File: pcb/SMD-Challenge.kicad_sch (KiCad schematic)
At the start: 1 part

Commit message: Add first draft
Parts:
- removed R?: (no value), symbol Device:R
- added BT1: Battery_Cell, Battery:BatteryHolder_Keystone_3002_1x2032, symbol Device:Battery_Cell
- added C1: 1u, Capacitor_SMD:C_1206_3216Metric, symbol Device:C
- added D1, D2: LED, LED_SMD:LED_1206_3216Metric, symbol Device:LED
- added D10, D9: LED, LED_SMD:LED_0201_0603Metric, symbol Device:LED
- added D3, D4: LED, LED_SMD:LED_0805_2012Metric, symbol Device:LED
- added D5, D6: LED, LED_SMD:LED_0603_1608Metric, symbol Device:LED
- added D7, D8: LED, LED_SMD:LED_0402_1005Metric, symbol Device:LED
- added R1, R2: R, Resistor_SMD:R_1206_3216Metric, symbol Device:R
- added R10, R9: R, Resistor_SMD:R_0201_0603Metric, symbol Device:R
- added R11: (no value), Resistor_SMD:R_1206_3216Metric, symbol Device:R
- added R3, R4: R, Resistor_SMD:R_0805_2012Metric, symbol Device:R
- added R5, R6: R, Resistor_SMD:R_0603_1608Metric, symbol Device:R
- added R7, R8: R, Resistor_SMD:R_0402_1005Metric, symbol Device:R
- added RV1: 100k, Potentiometer_SMD:Potentiometer_Bourns_TC33X_Vertical, symbol Device:R_Potentiometer
- added U1: SN74LVC1G14DBV, Package_TO_SOT_SMD:SOT-23-5, symbol 74xGxx:SN74LVC1G14DBV
- added U2: 4017, Package_SO:SO-16_3.9x9.9mm_P1.27mm, symbol 4xxx:4017
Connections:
- new net: R6.1, U2.10 (Q4)
- new net: D6.2 (A), R6.2
- new net: R7.1, U2.7 (Q3)
- new net: D7.2 (A), R7.2
- new net: R1.1, U2.11 (Q9)
- new net: D1.2 (A), R1.2
- new net: D10.2 (A), R10.2
- new net: R3.1, U2.6 (Q7)
- new net: D3.2 (A), R3.2
- new net: D8.2 (A), R8.2
- new net: C1.1, R11.1, U1.2
- new net: RV1.1, RV1.2, U1.4, U2.14 (CLK)
- new net: R11.2, RV1.3
- new net: R4.1, U2.5 (Q6)
- new net: D4.2 (A), R4.2
- new net: D9.2 (A), R9.2
- new net: D2.2 (A), R2.2
- new net: R5.1, U2.1 (Q5)
- new net: D5.2 (A), R5.2
- new net: R2.1, U2.9 (Q8)
- new net: R9.1, U2.2 (Q1)
- new net: R8.1, U2.4 (Q2)
- new net: R10.1, U2.3 (Q0)
- new net GND: BT1.2 (-), C1.2, D1.1 (K), D10.1 (K), D2.1 (K), D3.1 (K), D4.1 (K), D5.1 (K), D6.1 (K), D7.1 (K), D8.1 (K), D9.1 (K), U1.3 (GND), U2.13 (CKEN), U2.15 (Reset), U2.8 (VSS)
- new net VCC: BT1.1 (+), U1.5 (VCC), U2.16 (VDD)
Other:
- note added: "0201"
- note added: "0402"
- note added: "0603"
- note added: "0805"
- note added: "1206"
- company: Chris -> (c) by C. Zaugg

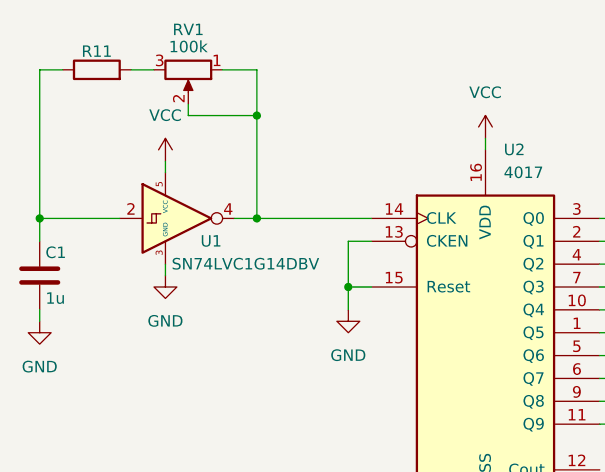
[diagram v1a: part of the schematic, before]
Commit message: Update to KiCad7
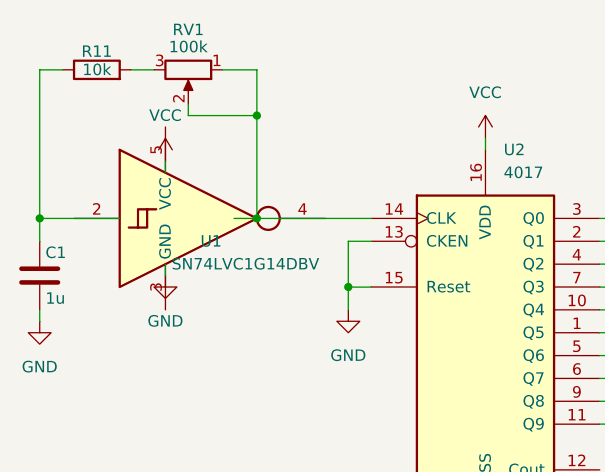
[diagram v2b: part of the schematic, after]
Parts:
- R11: value (none) -> 10k
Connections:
- net GND: no longer U1.3 (GND)
- net VCC: no longer U1.5 (VCC)
- net at U1.1 (NC): now also RV1.1, RV1.2, U2.14 (CLK)
- net at C1.1, R11.1: no longer U1.2
- now unconnected: U1.4

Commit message: Updated design
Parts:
- removed R1, R2: R, Resistor_SMD:R_1206_3216Metric, symbol Device:R
- removed R10, R9: R, Resistor_SMD:R_0201_0603Metric, symbol Device:R
- removed R3, R4: R, Resistor_SMD:R_0805_2012Metric, symbol Device:R
- removed R5, R6: R, Resistor_SMD:R_0603_1608Metric, symbol Device:R
- removed R7, R8: R, Resistor_SMD:R_0402_1005Metric, symbol Device:R
- added H1: MountingHole, MountingHole:MountingHole_2.2mm_M2, symbol Mechanical:MountingHole
- added SW1: SW_SPDT, Button_Switch_SMD:SW_SPDT_PCM12, symbol Switch:SW_SPDT
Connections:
- net GND: now also U1.3 (GND)
- net VCC: now also U1.5 (VCC), SW1.1 (A); no longer BT1.1 (+)
- net at U2.10 (Q4): now also D6.2 (A)
- net at U2.7 (Q3): now also D7.2 (A)
- net at U2.11 (Q9): now also D1.2 (A)
- net at D10.2 (A): now also U2.3 (Q0)
- net at U2.6 (Q7): now also D3.2 (A)
- net at D8.2 (A): now also U2.4 (Q2)
- net at RV1.1, RV1.2, U2.14 (CLK): now also U1.4; no longer U1.1 (NC)
- net at U1.2: now also C1.1, R11.1
- net at U2.5 (Q6): now also D4.2 (A)
- net at D9.2 (A): now also U2.2 (Q1)
- net at D2.2 (A): now also U2.9 (Q8)
- net at U2.1 (Q5): now also D5.2 (A)
- new net: BT1.1 (+), SW1.2 (B)
- no-connect marks 0 -> 2
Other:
- moved on the sheet: BT1, D1, D10, D2, D3, D4, D5, D6, D7, D8, D9, R11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
